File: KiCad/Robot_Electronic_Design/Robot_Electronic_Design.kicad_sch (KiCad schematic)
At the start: 3 parts, among them J1 Conn_01x19_Female, J2 Conn_01x19_Female, U1 L298N

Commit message: Update Kicad Files
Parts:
- removed U1: L298N, Package_TO_SOT_THT:TO-220-15_P2.54x2.54mm_StaggerOdd_Lead4.58mm_Vertical, symbol Driver_Motor:L298N
- added BT1, BT2: 3.7V, symbol Device:Battery_Cell
- added C1, C2: 10uF, Capacitor_THT:CP_Radial_D5.0mm_P2.00mm, symbol Device:C_Polarized
- added M1, M2: Motor_DC, Connector_PinHeader_2.00mm:PinHeader_2x01_P2.00mm_Vertical, symbol Motor:Motor_DC
- added M3: Water Pump, Connector_PinHeader_2.00mm:PinHeader_2x01_P2.00mm_Vertical, symbol Motor:Motor_DC
- added SW1: SW_SPST, symbol Switch:SW_SPST
- added U2: NEO-6M, NEO-6M:NEO-6M, symbol NEO-6M:NEO-6M
- added U3, U4, U5: HC-SR04, HC-SR04:XCVR_HC-SR04, symbol HC-SR04:HC-SR04
- added U6: L298N, Package_TO_SOT_THT:TO-220-15_P2.54x2.54mm_StaggerOdd_Lead4.58mm_Vertical, symbol Driver_Motor:L298N
- added U7, U8: LM393, symbol Comparator:LM393
- added U9: AMS1117-5.0, Package_TO_SOT_SMD:SOT-223-3_TabPin2, symbol Regulator_Linear:AMS1117-5.0
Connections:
- net 3.3V: now also J1.3V3 (Pin_1), U2.4 (VCC); no longer J1.1 (Pin_1)
- removed net ESP_GND: J1.14 (Pin_14), J2.1 (Pin_1), J2.7 (Pin_7)
- removed net M11: J1.9 (Pin_9)
- removed net M12: J1.10 (Pin_10)
- removed net M21: J2.8 (Pin_8)
- removed net M22: J2.9 (Pin_9)
- removed net Vcc: J1.19 (Pin_19)
- new net ECHO_1: J1.D21 (Pin_11), U3.3 (ECHO)
- new net ECHO_2: J1.D23 (Pin_15), U4.3 (ECHO)
- new net ECHO_3: J2.D26 (Pin_7), U5.3 (ECHO)
- new net ENA: J1.D5 (Pin_8), U6.6 (EnA)
- new net ENB: J1.D15 (Pin_3), U6.11 (EnB)
- new net ESP32_RX: J1.TX0 (Pin_13), U2.2 (TX)
- new net ESP32_TX: J1.RX0 (Pin_12), U2.3 (RX)
- new net GND: BT1.2 (-), BT2.2 (-), C1.2, C2.2, SW1.2 (B), U2.1 (GND), U3.4 (GND), U4.4 (GND), U5.4 (GND), U6.8 (GND), U9.1 (GND)
- new net IN1: J1.D16 (Pin_6), U6.5 (IN1)
- new net IN2: J1.D17 (Pin_7), U6.7 (IN2)
- new net IN3: J1.D4 (Pin_5), U6.10 (IN3)
- new net IN4: J1.D2 (Pin_4), U6.12 (IN4)
- new net MOTOR_1_OUT1: M1.1 (+), U6.2 (OUT1)
- new net MOTOR_1_OUT2: M1.2 (-), U6.3 (OUT2)
- new net MOTOR_2_OUT1: M2.1 (+), U6.13 (OUT3)
- new net MOTOR_2_OUT2: M2.2 (-), U6.14 (OUT4)
- new net TRIG_1: J1.D19 (Pin_10), U3.2 (TRIG)
- new net TRIG_2: J1.D22 (Pin_14), U4.2 (TRIG)
- new net TRIG_3: J2.D25 (Pin_8), U5.2 (TRIG)
- new net VCC: BT1.1 (+), BT2.1 (+), C1.1, SW1.1 (A), U6.4 (Vs), U9.3 (VI)
- new net Vin: C2.1, J2.Vin (Pin_1), U3.1 (VCC), U4.1 (VCC), U5.1 (VCC), U6.9 (Vss), U9.2 (VO)
- no-connect marks 0 -> 2
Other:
- note added: "AMS1117 Regulator"
- note added: "Actuators"
- note added: "ESP32-DEVKIT-C"
- note added: "Flame Sensor (KY-026)"
- note added: "GPS Module (NEO-6M)"
- note added: "L298N Driver"
- note added: "MCU"
- note added: "Power DC"
- note added: "Sensors"
- note added: "Ultrasonic Sensor (HC-SR04)"
- note removed: "esp32"
- company: (none) -> Facultad de Ingeniería Mecánica y Eléctrica
- title: (none) -> IoT Autonomous Fire Detection and Firefighting System

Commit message: test: DC Motors
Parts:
- U2: value NEO-6M -> NEO-7M; footprint NEO-6M:NEO-6M -> NEO-7M:NEO-7M; MP NEO-6M -> NEO-7M
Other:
- note added: "GPS Module (NEO-7M)"
- note removed: "GPS Module (NEO-6M)"
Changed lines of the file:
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@@
 		)
 	)
-	(text "GPS Module (NEO-6M)"
+	(text "GPS Module (NEO-7M)"
 		(exclude_from_sim no)
 		(at 34.544 202.438 0)
@@
 			)
 		)
-		(property "Value" "NEO-6M"
+		(property "Value" "NEO-7M"
 			(at 36.83 210.82 0)
 			(effects
@@
 			)
 		)
-		(property "Footprint" "NEO-6M:NEO-6M"
+		(property "Footprint" "NEO-7M:NEO-7M"
 			(at 45.72 213.36 0)
 			(effects
@@
 			)
 		)
-		(property "MP" "NEO-6M"
+		(property "MP" "NEO-7M"
 			(at 45.72 213.36 0)
 			(effects

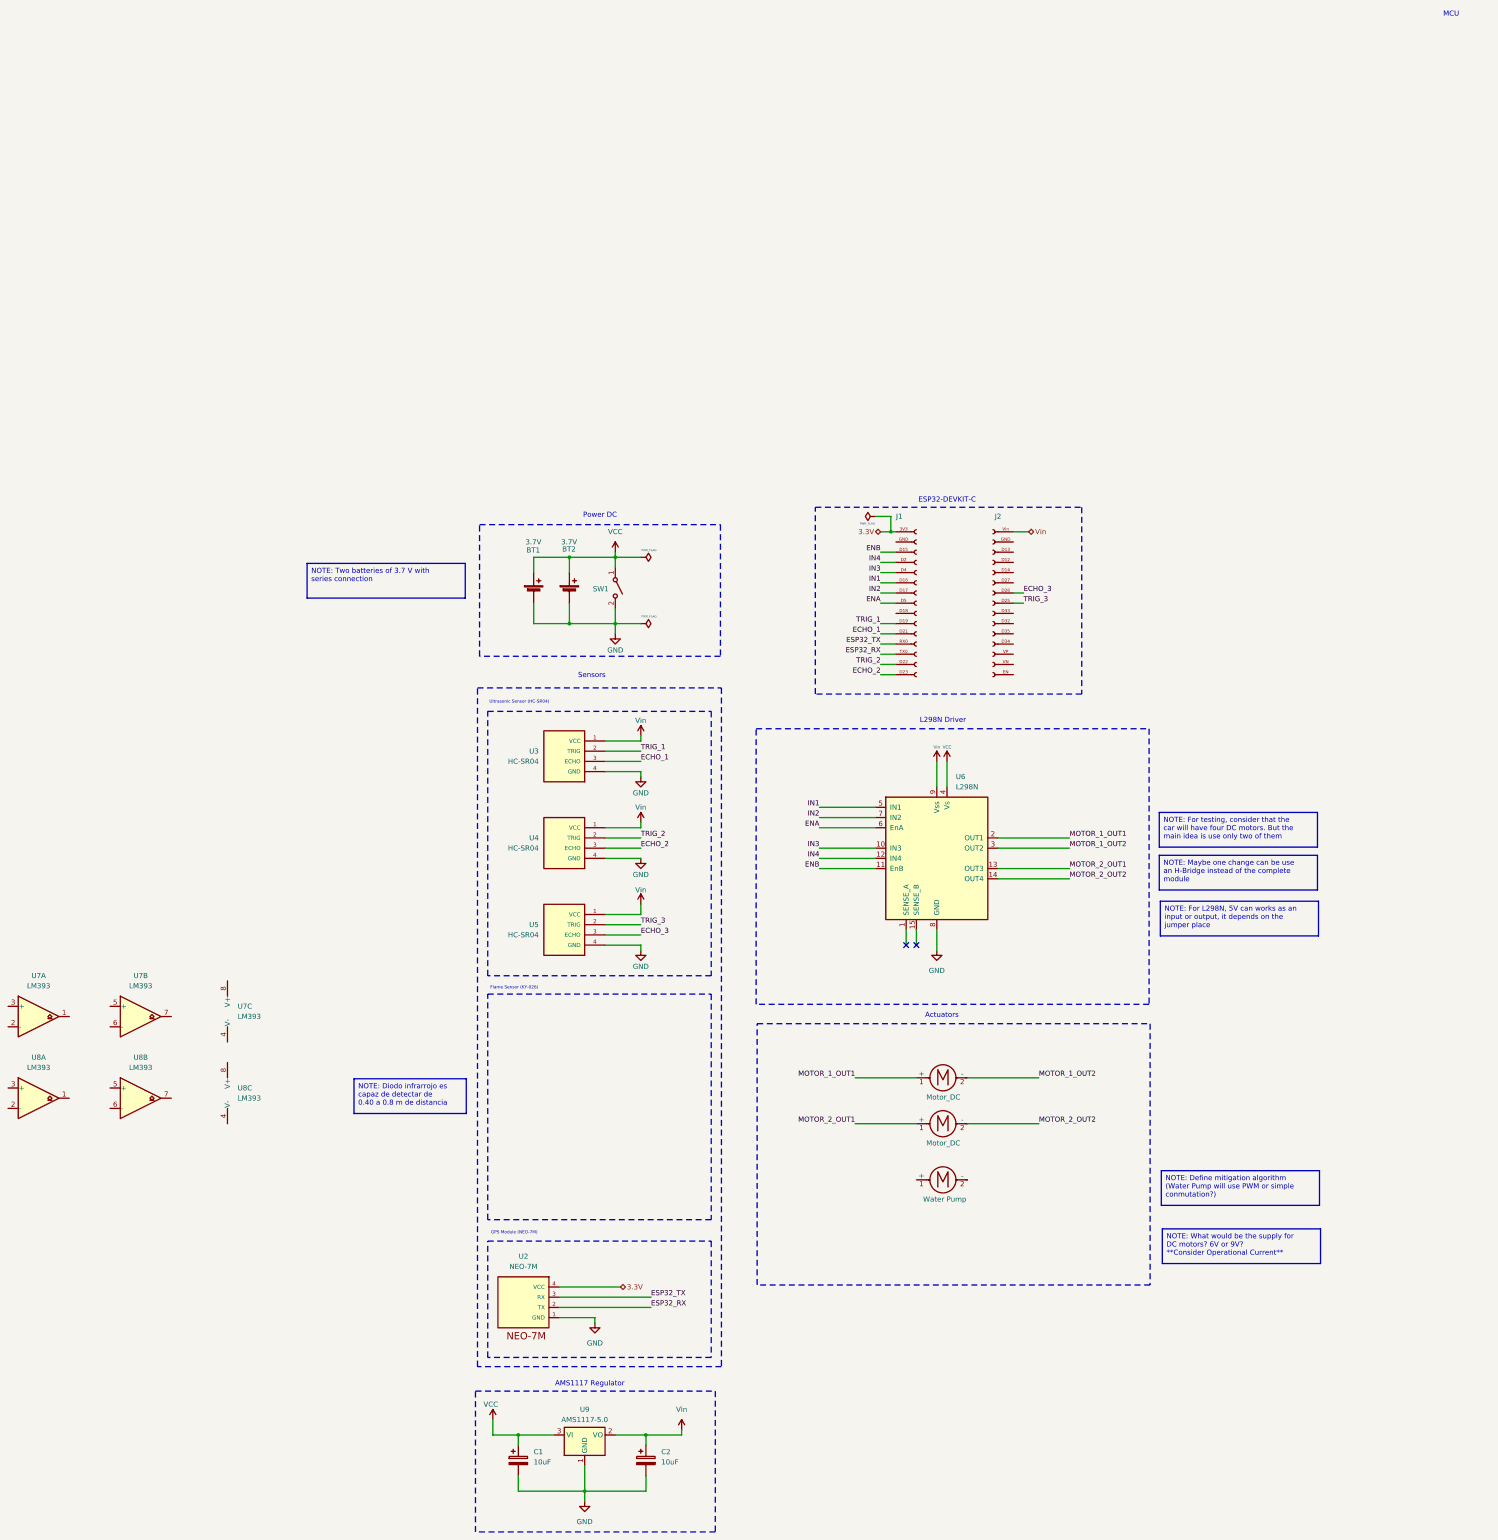
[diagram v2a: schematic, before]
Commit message: feat: Adding Compass Calibration
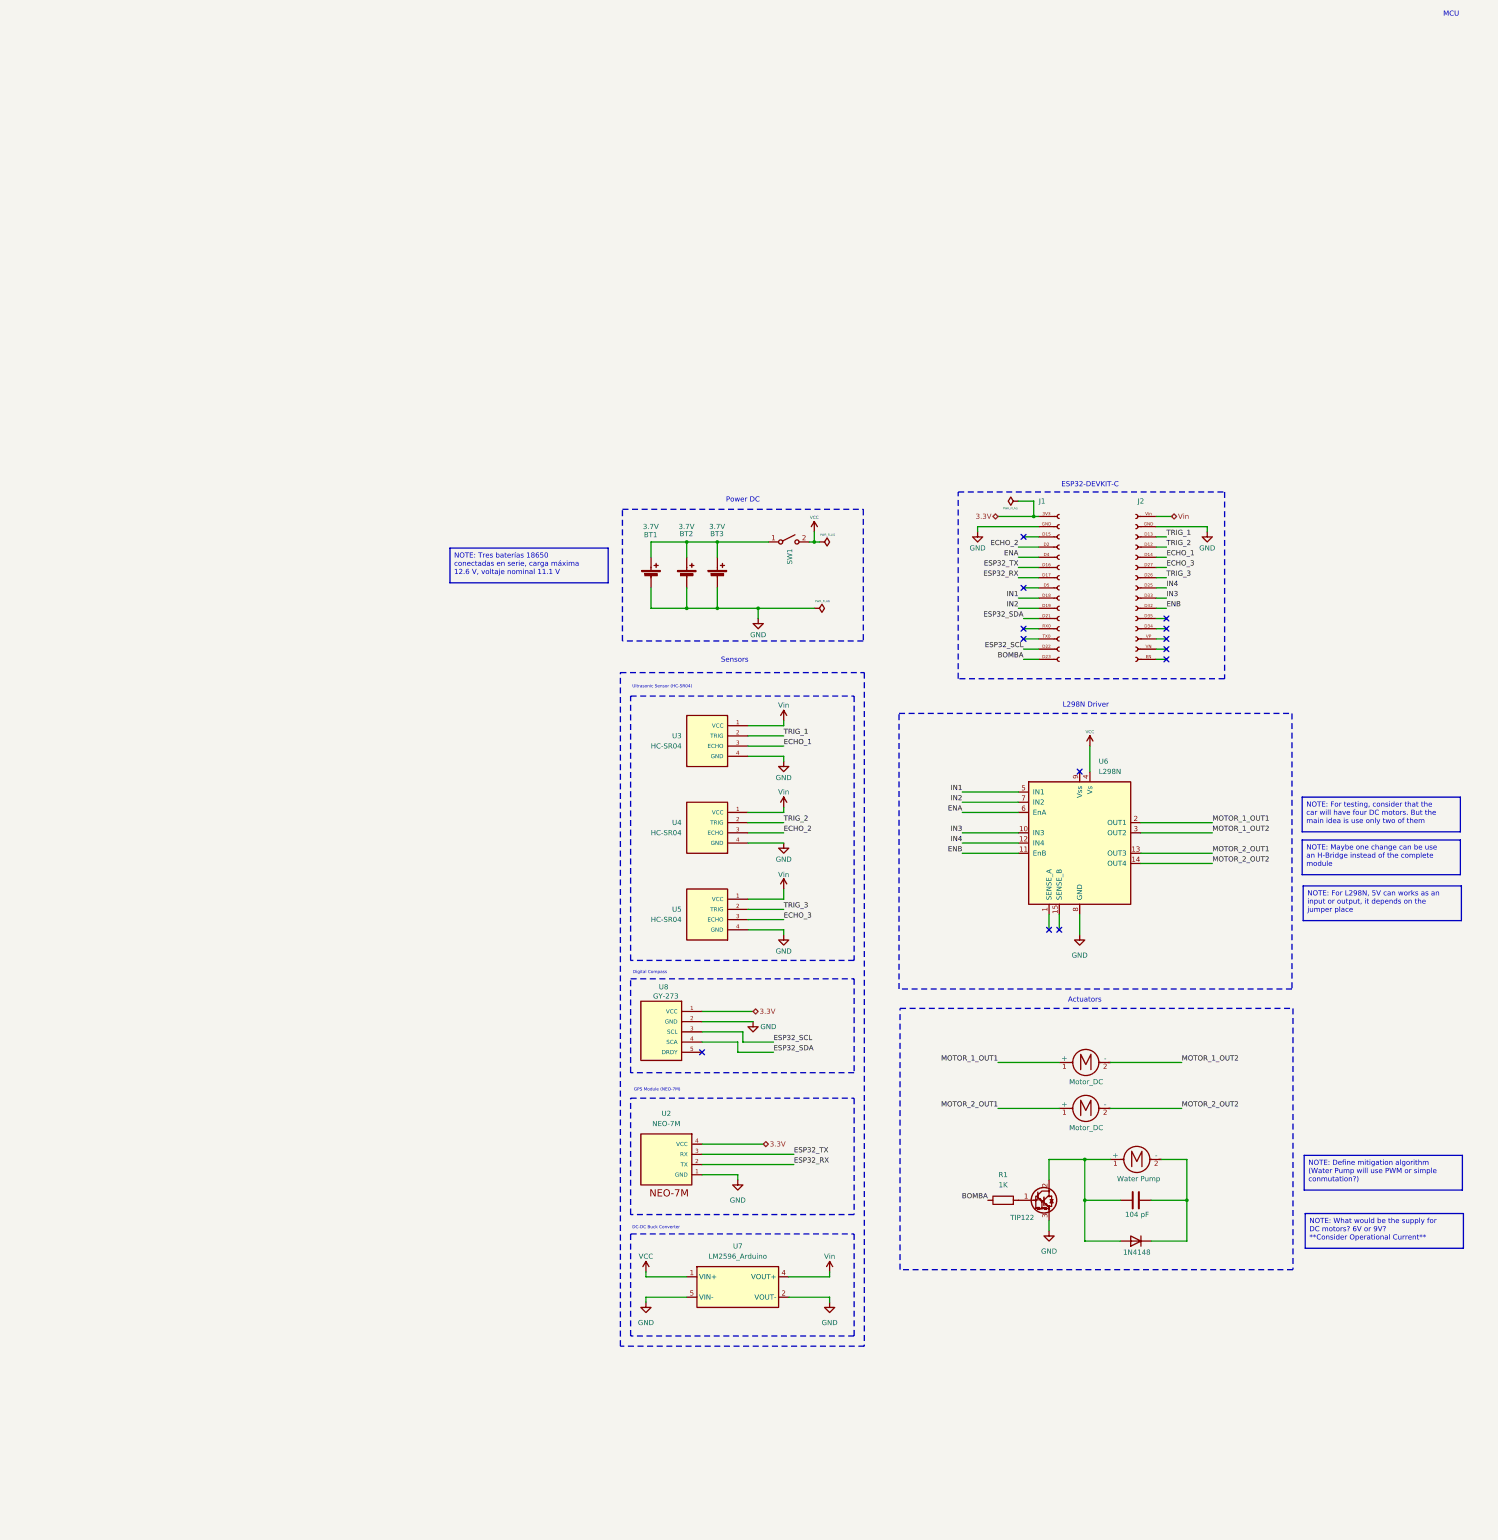
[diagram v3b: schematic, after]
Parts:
- removed C1, C2: 10uF, Capacitor_THT:CP_Radial_D5.0mm_P2.00mm, symbol Device:C_Polarized
- removed U7, U8: LM393, symbol Comparator:LM393
- removed U9: AMS1117-5.0, Package_TO_SOT_SMD:SOT-223-3_TabPin2, symbol Regulator_Linear:AMS1117-5.0
- added BT3: 3.7V, symbol Device:Battery_Cell
- added C1: 104 pF, symbol Device:C
- added D1: 1N4148, Diode_THT:D_DO-35_SOD27_P7.62mm_Horizontal, symbol Diode:1N4148
- added Q1: TIP122, Package_TO_SOT_THT:TO-220-3_Vertical, symbol Transistor_BJT:TIP122
- added R1: 1K, symbol Device:R
- added U7: LM2596_Arduino, Package_TO_SOT_SMD:TO-263-5_TabPin3, symbol 2596:LM2596_Arduino
- added U8: GY-273, HC-SR04:XCVR_HC-SR04, symbol GY273:GY-273
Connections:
- net 3.3V: now also U8.1 (VCC)
- net ECHO_1: now also J2.D14 (Pin_5); no longer J1.D21 (Pin_11)
- net ECHO_2: now also J1.D2 (Pin_4); no longer J1.D23 (Pin_15)
- net ECHO_3: now also J2.D27 (Pin_6); no longer J2.D26 (Pin_7)
- net ENA: now also J1.D4 (Pin_5); no longer J1.D5 (Pin_8)
- net ENB: now also J2.D32 (Pin_10); no longer J1.D15 (Pin_3)
- net ESP32_RX: now also J1.D17 (Pin_7); no longer J1.TX0 (Pin_13)
- net ESP32_TX: now also J1.D16 (Pin_6); no longer J1.RX0 (Pin_12)
- net GND: now also J1.GND (Pin_2), J2.GND (Pin_2), BT3.2 (-), Q1.3 (E), U7.2 (VOUT-), U7.5 (VIN-), U8.2 (GND); no longer SW1.2 (B)
- net IN1: now also J1.D18 (Pin_9); no longer J1.D16 (Pin_6)
- net IN2: now also J1.D19 (Pin_10); no longer J1.D17 (Pin_7)
- net IN3: now also J2.D33 (Pin_9); no longer J1.D4 (Pin_5)
- net IN4: now also J2.D25 (Pin_8); no longer J1.D2 (Pin_4)
- net TRIG_1: now also J2.D13 (Pin_3); no longer J1.D19 (Pin_10)
- net TRIG_2: now also J2.D12 (Pin_4); no longer J1.D22 (Pin_14)
- net TRIG_3: now also J2.D26 (Pin_7); no longer J2.D25 (Pin_8)
- net VCC: now also SW1.2 (B), U7.1 (VIN+); no longer BT1.1 (+), BT2.1 (+), SW1.1 (A)
- net Vin: now also U7.4 (VOUT+); no longer U6.9 (Vss)
- net at M3.1 (+): now also C1.1, D1.2 (A), Q1.2 (C)
- net at M3.2 (-): now also C1.2, D1.1 (K)
- new net: BT1.1 (+), BT2.1 (+), BT3.1 (+), SW1.1 (A)
- new net: Q1.1 (B), R1.2
- new net BOMBA: J1.D23 (Pin_15), R1.1
- new net ESP32_SCL: J1.D22 (Pin_14), U8.3 (SCL)
- new net ESP32_SDA: J1.D21 (Pin_11), U8.4 (SCA)
- no-connect marks 2 -> 13
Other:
- note added: "DC-DC Buck Converter"
- note added: "Digital Compass"
- note removed: "AMS1117 Regulator"
- note removed: "Flame Sensor (KY-026)"
- moved on the sheet: BT1, BT2, J1, J2, SW1, U2, U3, U4, U5, U6
